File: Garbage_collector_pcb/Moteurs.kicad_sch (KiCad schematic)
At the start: 11 parts, among them J1 Connecteur moteur 1, J3 Connecteur moteur 2, J4 Conn_Servo1, J5 Conn_Servo2, J6 Conn_Servo3, U1 DRV8833PWP

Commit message: seance 24 septembre
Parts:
- removed J1: Connecteur moteur 1, Connector_JST:JST_EH_S6B-EH_1x06_P2.50mm_Horizontal, symbol Connector:Conn_01x06_Pin
- removed J3: Connecteur moteur 2, Connector_JST:JST_EH_S6B-EH_1x06_P2.50mm_Horizontal, symbol Connector:Conn_01x06_Pin
- removed J4: Conn_Servo1, Connector_JST:JST_EH_S3B-EH_1x03_P2.50mm_Horizontal, symbol Connector:Conn_01x03_Pin
- removed J5: Conn_Servo2, Connector_JST:JST_EH_S3B-EH_1x03_P2.50mm_Horizontal, symbol Connector:Conn_01x03_Pin
- removed J6: Conn_Servo3, Connector_JST:JST_EH_S3B-EH_1x03_P2.50mm_Horizontal, symbol Connector:Conn_01x03_Pin
- added J1, J3: Conn_01x06, symbol Kicad:Conn_01x06
- added J11, J13, J14: Conn_01x03, symbol Kicad:Conn_01x03
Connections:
- net VM is gone; now on net +5V: C11.1, C2.1, U1.12 (VM)
- net +5V: now also J1.3 (Pin_3), J11.2 (Pin_2), J13.2 (Pin_2), J14.2 (Pin_2), J3.3 (Pin_3)
- net GND: now also C1.2, J1.6 (Pin_6), J11.1 (Pin_1), J13.1 (Pin_1), J14.1 (Pin_1), J3.6 (Pin_6); no longer C1.1
- net M1_ENCA: now also J1.4 (Pin_4)
- net M1_ENCB: now also J1.5 (Pin_5)
- net M2_ENCA: now also J3.4 (Pin_4)
- net M2_ENCB: now also J3.5 (Pin_5)
- net at U1.14 (VINT): now also C1.1; no longer C1.2
- net M1_OUT1 renamed AOUT1
- net AOUT1: now also J1.1 (Pin_1)
- net M1_OUT2 renamed AOUT2
- net AOUT2: now also J1.2 (Pin_2)
- net M2_OUT1 renamed BOUT1
- net BOUT1: now also J3.1 (Pin_1)
- net M2_OUT2 renamed BOUT2
- net BOUT2: now also J3.2 (Pin_2)
- new net Servo1: J11.3 (Pin_3)
- new net Servo2: J13.3 (Pin_3)
- new net Servo3: J14.3 (Pin_3)
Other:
- moved on the sheet: C2, R2, U1

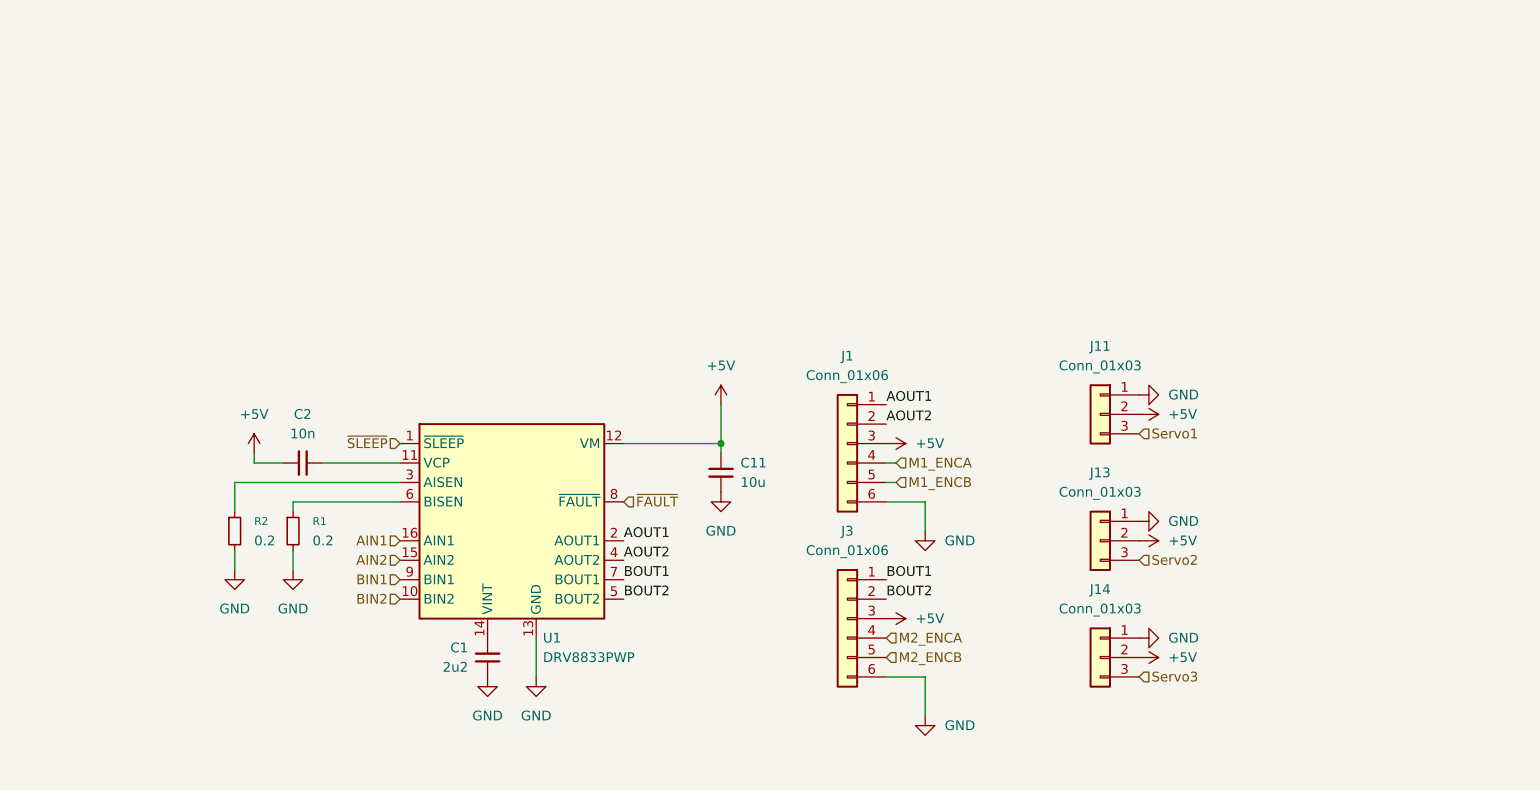
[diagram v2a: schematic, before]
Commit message: update schematic
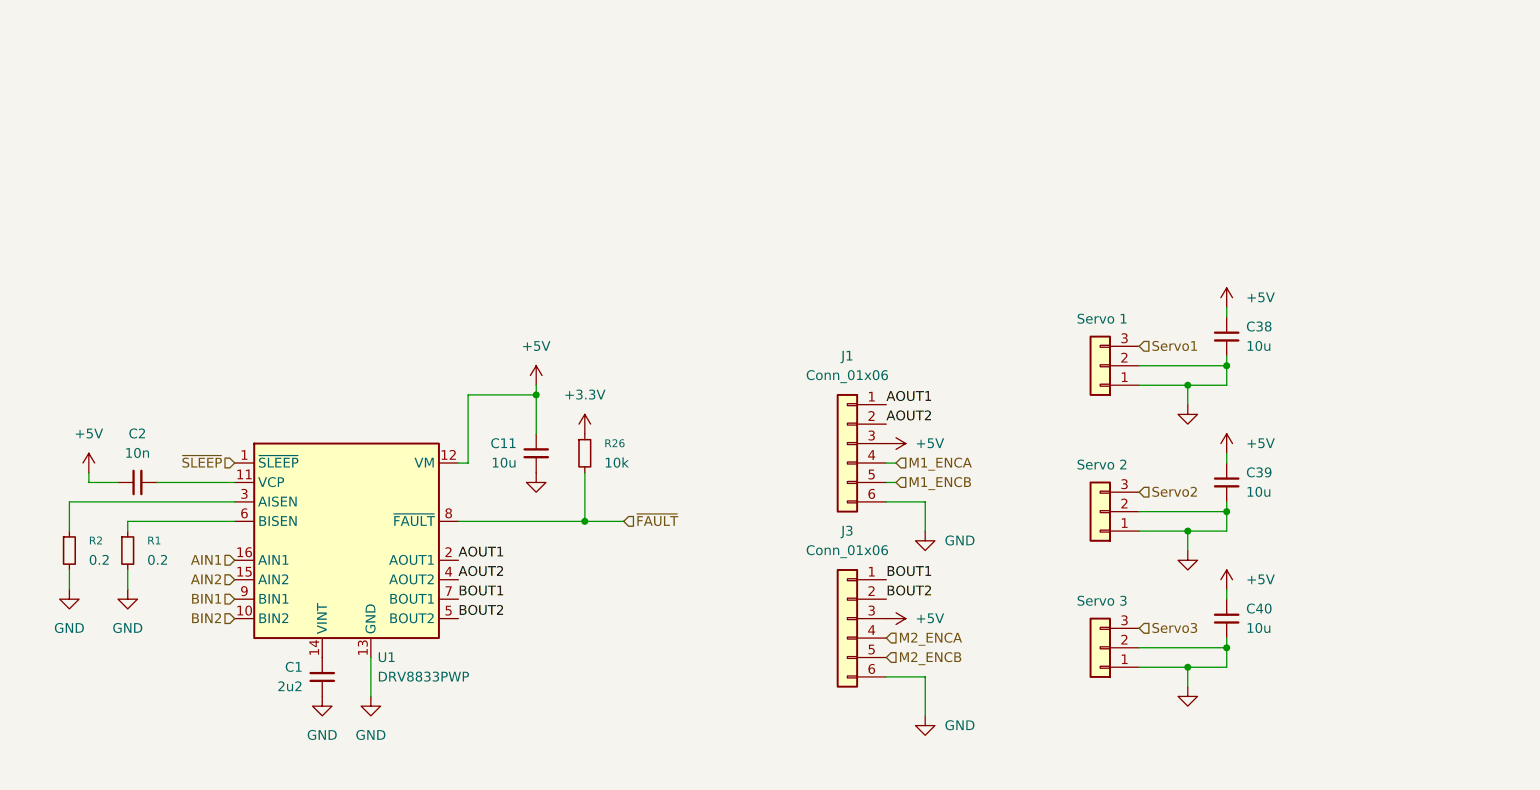
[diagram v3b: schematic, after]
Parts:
- added C38, C39, C40: 10u, Capacitor_SMD:C_0603_1608Metric, symbol Device:C_Small
- added R26: 10k, Resistor_SMD:R_0402_1005Metric, symbol Device:R_Small
- J11: value Conn_01x03 -> Servo 1; footprint (none) -> Connector_PinHeader_2.54mm:PinHeader_1x03_P2.54mm_Vertical
- J13: value Conn_01x03 -> Servo 2; footprint (none) -> Connector_PinHeader_2.54mm:PinHeader_1x03_P2.54mm_Vertical
- J14: value Conn_01x03 -> Servo 3; footprint (none) -> Connector_PinHeader_2.54mm:PinHeader_1x03_P2.54mm_Vertical
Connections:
- net +5V: now also C38.1, C39.1, C40.1; no longer J11.2 (Pin_2), J13.2 (Pin_2), J14.2 (Pin_2)
- net GND: now also J11.2 (Pin_2), J13.2 (Pin_2), J14.2 (Pin_2), C38.2, C39.2, C40.2
- net ~{FAULT}: now also R26.2
- new net +3.3V: R26.1
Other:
- moved on the sheet: C1, C11, C2, R1, R2, U1

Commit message: update MCU+Moteurs+Capteurs parts + assignement des labels + assignement des pins sur l'ioc (CubeMX)
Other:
- note added: "Connecteurs Moteurs DC"
- note added: "Connecteurs Servomoteurs"
- note added: "Driver Moteurs DC"
- moved on the sheet: C38, C39, C40, J1, J3

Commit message: update schematic
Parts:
- removed C1: 2u2, Package_SO:HTSSOP-16-1EP_4.4x5mm_P0.65mm_EP3.4x5mm_Mask2.46x2.31mm_ThermalVias, symbol Device:C_Small
- removed C11: 10u, Package_SO:HTSSOP-16-1EP_4.4x5mm_P0.65mm_EP3.4x5mm_Mask2.46x2.31mm_ThermalVias, symbol Device:C_Small
- removed C2: 10n, Package_SO:HTSSOP-16-1EP_4.4x5mm_P0.65mm_EP3.4x5mm_Mask2.46x2.31mm_ThermalVias, symbol Device:C_Small
- removed J3: Conn_01x06, symbol Kicad:Conn_01x06
- removed R2: 0.2, Resistor_THT:R_Array_SIP4, symbol Device:R_Small
- added C16: 10u, symbol Kicad:C_Polarized_Small
- added C17: 10u, Capacitor_SMD:C_0603_1608Metric, symbol Device:C_Small
- added C22: 2u2, Capacitor_SMD:C_0402_1005Metric, symbol Device:C_Small
- added C24, C26: 100n, Capacitor_SMD:C_0402_1005Metric, symbol Device:C_Small
- added J14, J15: Conn_01x06, symbol Kicad:Conn_01x06
- added R36: 0.2, Resistor_THT:R_Array_SIP4, symbol Device:R_Small
- R28: renamed from R1; JLCPCB Part # (none) -> C171371
- renumbered C38 to C32, C39 to C33, C40 to C34, J1 to J3, J11 to J5, J13 to J6, J14 to J7, R26 to R29, U1 to U4
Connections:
- net +3.3V: now also C24.1, C26.1, J14.2 (Pin_2), J15.2 (Pin_2)
- net +5V: now also C16.1, C17.1
- net AOUT1: now also J14.1 (Pin_1)
- net AOUT2: now also J14.6 (Pin_6)
- net BOUT1: now also J15.1 (Pin_1)
- net BOUT2: now also J15.6 (Pin_6)
- net GND: now also C16.2, C22.2, C24.2, C26.2, J14.5 (Pin_5), J15.5 (Pin_5), R36.2
- net M1_ENCA: now also J14.3 (Pin_3)
- net M1_ENCB: now also J14.4 (Pin_4)
- net M2_ENCA: now also J15.3 (Pin_3)
- net M2_ENCB: now also J15.4 (Pin_4)
- net at U4.3 (AISEN): now also R36.1
- net at U4.14 (VINT): now also C22.1
- net at U4.11 (VCP): now also C17.2
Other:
- moved on the sheet: J3, R29

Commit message: ajout du ioc et schema validé
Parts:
- removed C16: 10u, symbol Kicad:C_Polarized_Small
- removed C34: 10u, Capacitor_SMD:C_0603_1608Metric, symbol Device:C_Small
- removed J14, J15, J3: Conn_01x06, symbol Kicad:Conn_01x06
- removed J5: Servo 1, Connector_PinHeader_2.54mm:PinHeader_1x03_P2.54mm_Vertical, symbol Kicad:Conn_01x03
- removed J6: Servo 2, Connector_PinHeader_2.54mm:PinHeader_1x03_P2.54mm_Vertical, symbol Kicad:Conn_01x03
- removed J7: Servo 3, Connector_PinHeader_2.54mm:PinHeader_1x03_P2.54mm_Vertical, symbol Kicad:Conn_01x03
- added C27: 10u, Capacitor_SMD:C_0603_1608Metric, symbol Device:C_Small
- added C3: 470u, Capacitor_SMD:CP_Elec_10x10.5, symbol Kicad:C_Polarized_Small
- added J12: MOTOR2, Connector_JST:JST_GH_SM06B-GHS-TB_1x06-1MP_P1.25mm_Horizontal, symbol Connector_Generic:Conn_01x06
- added J13: MOTOR1, Connector_JST:JST_GH_SM06B-GHS-TB_1x06-1MP_P1.25mm_Horizontal, symbol Connector_Generic:Conn_01x06
- added J5: SERVO1, Connector_JST:JST_GH_SM03B-GHS-TB_1x03-1MP_P1.25mm_Horizontal, symbol Connector_Generic:Conn_01x03
- added J6: SERVO2, Connector_JST:JST_GH_SM03B-GHS-TB_1x03-1MP_P1.25mm_Horizontal, symbol Connector_Generic:Conn_01x03
- C17: value 10u -> 10n
- R28, R36: value 0.2 -> 200m
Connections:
- net +3.3V: now also J12.2 (Pin_2), J13.2 (Pin_2)
- net +5V: now also C27.1, C3.1, J5.2 (Pin_2), J6.2 (Pin_2)
- net AOUT1: now also J13.1 (Pin_1)
- net AOUT2: now also J13.6 (Pin_6)
- net BOUT1: now also J12.1 (Pin_1)
- net BOUT2: now also J12.6 (Pin_6)
- net GND: now also C27.2, C3.2, J12.5 (Pin_5), J13.5 (Pin_5), J5.3 (Pin_3), J6.3 (Pin_3)
- net M1_ENCA: now also J13.3 (Pin_3)
- net M1_ENCB: now also J13.4 (Pin_4)
- net M2_ENCA: now also J12.3 (Pin_3)
- net M2_ENCB: now also J12.4 (Pin_4)
- net Servo1: now also J5.1 (Pin_1)
- net Servo2: now also J6.1 (Pin_1)
- net ~{FAULT} renamed MOTOR_FAULT
- net ~{SLEEP} renamed MOTOR_SLEEP
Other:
- moved on the sheet: C17, C22, C32, C33, R29

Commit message: finalisation des empreintes
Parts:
- renumbered C22 to C27, C27 to C28, C3 to C29, C17 to C30, C26 to C31, C24 to C32, C32 to C33, C33 to C34, J12 to J4, J13 to J5, J5 to J6, J6 to J7, R36 to R24, R28 to R25, R29 to R26

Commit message: routage du pcb quasiment terminé, 1 erreur DRC
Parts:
- R24, R25: footprint Resistor_THT:R_Array_SIP4 -> Resistor_SMD:R_0805_2012Metric
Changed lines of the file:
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@@
 			)
 		)
-		(property "Footprint" "Resistor_THT:R_Array_SIP4"
+		(property "Footprint" "Resistor_SMD:R_0805_2012Metric"
 			(at 25.4 86.36 0)
 			(hide yes)
@@
 			)
 		)
-		(property "Footprint" "Resistor_THT:R_Array_SIP4"
+		(property "Footprint" "Resistor_SMD:R_0805_2012Metric"
 			(at 17.78 86.36 0)
 			(hide yes)
